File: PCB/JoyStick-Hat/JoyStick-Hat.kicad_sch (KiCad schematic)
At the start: 0 parts

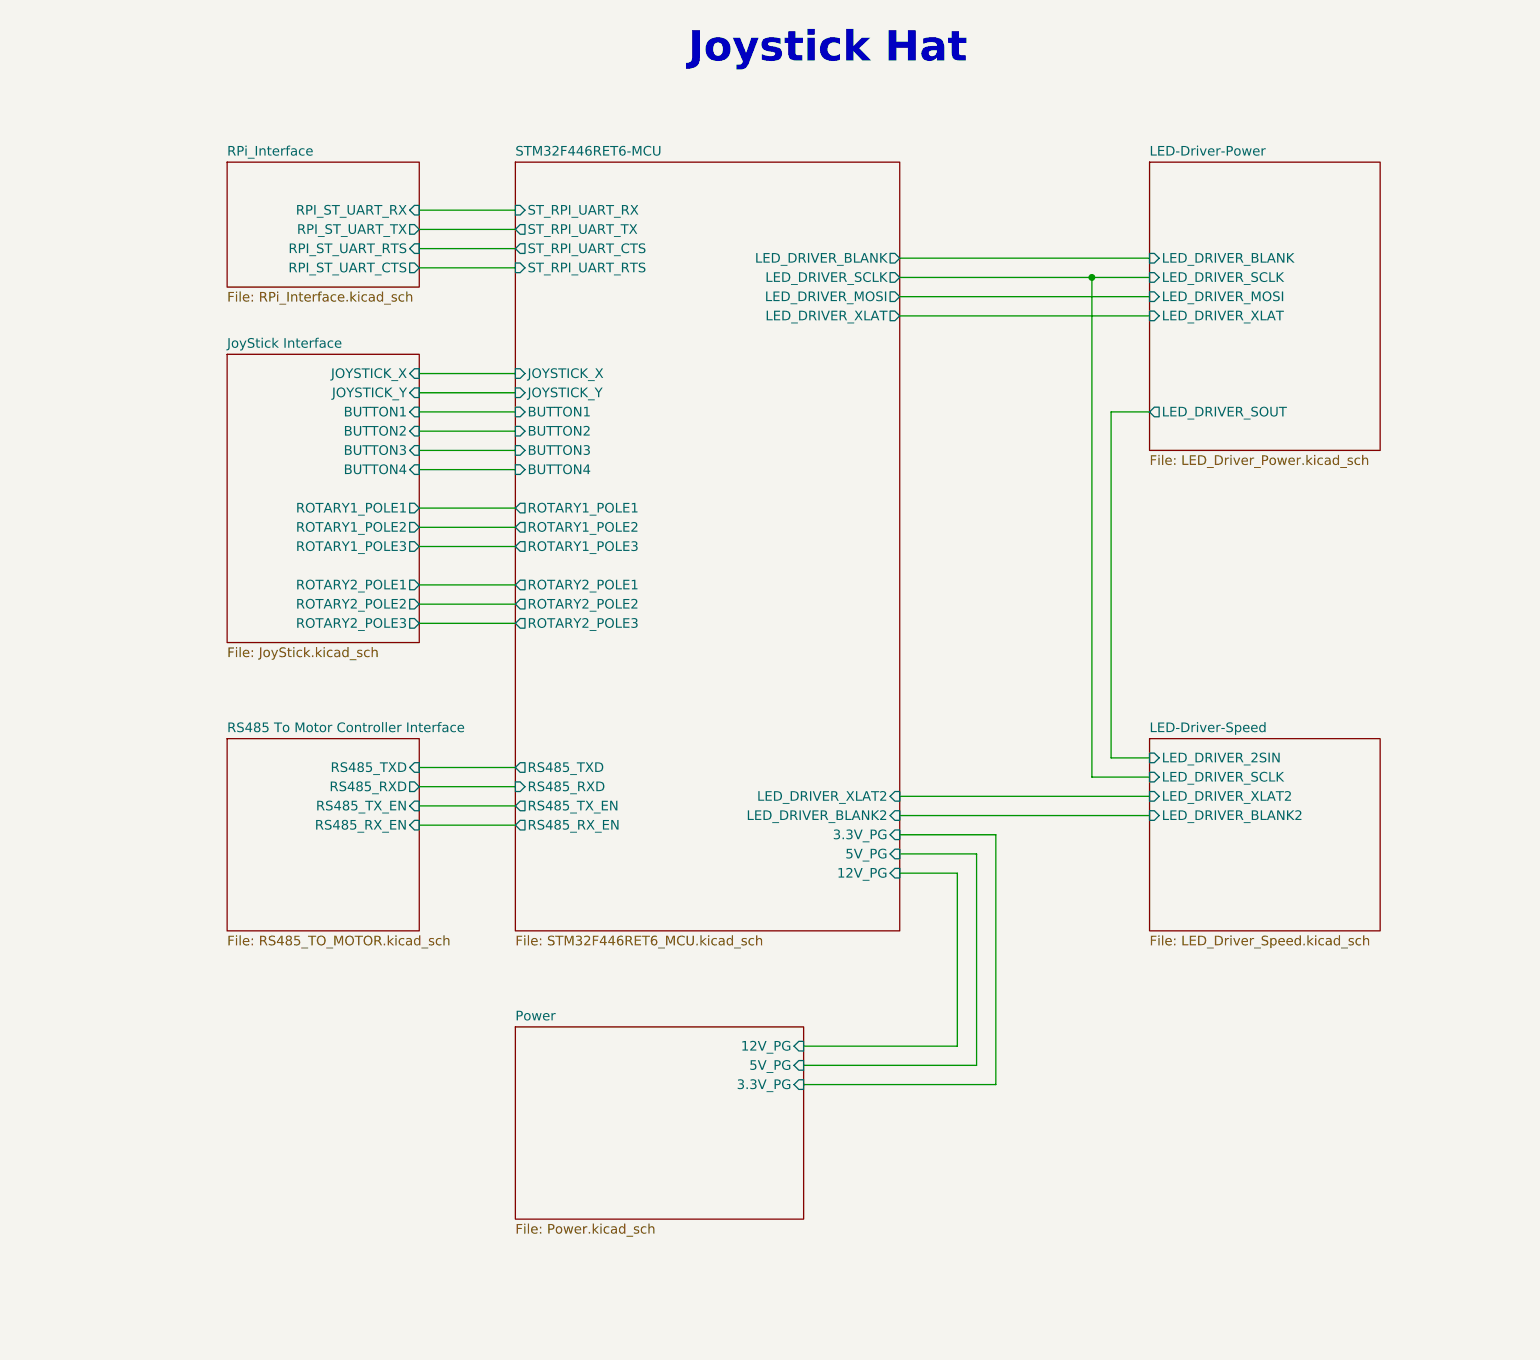
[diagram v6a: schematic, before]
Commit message: Design Rules, Component Placement. Features Dropped
Added design rules for OSHPark.com to PCB, Most components placed roughly for whole board more to follow and more tweaks,. Features were dropped/rearanged. USB for STM32 dropped as its not necessary. LED driver and LEDs will be on separate board and SPI will run through cabling via differential transceiver that has yet to be added to schematic.
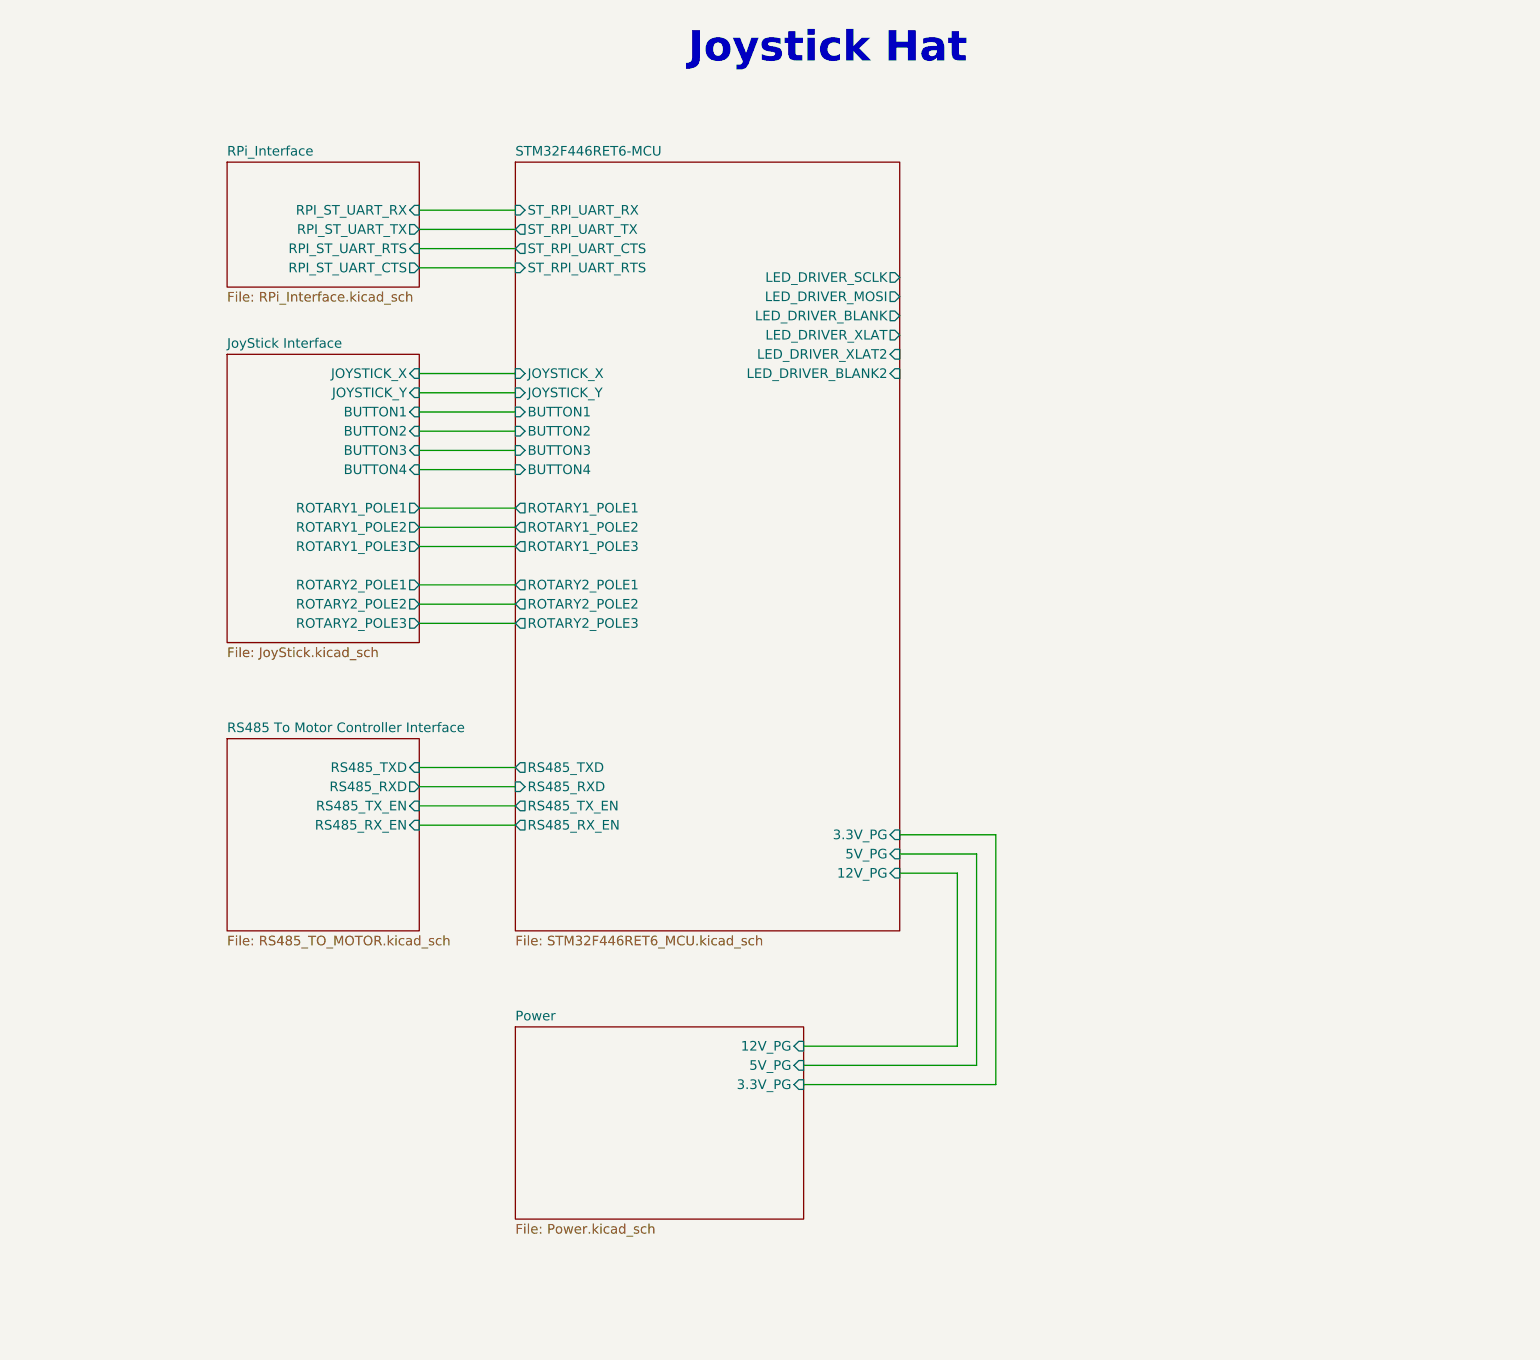
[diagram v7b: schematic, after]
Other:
- removed sheet LED-Driver-Power
- removed sheet LED-Driver-Speed
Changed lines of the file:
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@@
 (kicad_sch (version 20230121) (generator eeschema)
   (paper "A4")
-  (junction (at 190.5 53.34) (diameter 0) (color 0 0 0 0)
-  )
-  (wire (pts (xy 190.5 53.34) (xy 198.12 53.34))
-    (stroke (width 0) (type default))
-  )
   (wire (pts (xy 177.8 127) (xy 165.1 127))
     (stroke (width 0) (type default))
@@
     (stroke (width 0) (type default))
   )
-  (wire (pts (xy 165.1 58.42) (xy 198.12 58.42))
-    (stroke (width 0) (type default))
-  )
   (wire (pts (xy 101.6 86.36) (xy 114.3 86.36))
     (stroke (width 0) (type default))
@@
     (stroke (width 0) (type default))
   )
-  (wire (pts (xy 165.1 124.46) (xy 198.12 124.46))
-    (stroke (width 0) (type default))
-  )
   (wire (pts (xy 152.4 160.02) (xy 177.8 160.02))
     (stroke (width 0) (type default))
   )
-  (wire (pts (xy 193.04 71.12) (xy 198.12 71.12))
-    (stroke (width 0) (type default))
-  )
   (wire (pts (xy 101.6 71.12) (xy 114.3 71.12))
     (stroke (width 0) (type default))
   )
-  (wire (pts (xy 190.5 53.34) (xy 190.5 119.38))
-    (stroke (width 0) (type default))
-  )
   (wire (pts (xy 101.6 76.2) (xy 114.3 76.2))
     (stroke (width 0) (type default))
   )
-  (wire (pts (xy 165.1 121.92) (xy 198.12 121.92))
-    (stroke (width 0) (type default))
-  )
   (wire (pts (xy 177.8 160.02) (xy 177.8 127))
     (stroke (width 0) (type default))
   )
-  (wire (pts (xy 165.1 55.88) (xy 198.12 55.88))
-    (stroke (width 0) (type default))
-  )
   (wire (pts (xy 101.6 123.19) (xy 114.3 123.19))
     (stroke (width 0) (type default))
@@
     (stroke (width 0) (type default))
   )
-  (wire (pts (xy 190.5 119.38) (xy 198.12 119.38))
-    (stroke (width 0) (type default))
-  )
-  (wire (pts (xy 165.1 50.8) (xy 198.12 50.8))
-    (stroke (width 0) (type default))
-  )
-  (wire (pts (xy 198.12 116.84) (xy 193.04 116.84))
-    (stroke (width 0) (type default))
-  )
   (wire (pts (xy 175.26 157.48) (xy 175.26 129.54))
     (stroke (width 0) (type default))
@@
     (stroke (width 0) (type default))
   )
-  (wire (pts (xy 193.04 116.84) (xy 193.04 71.12))
-    (stroke (width 0) (type default))
-  )
   (wire (pts (xy 101.6 125.73) (xy 114.3 125.73))
     (stroke (width 0) (type default))
@@
   )
   (wire (pts (xy 101.6 49.53) (xy 114.3 49.53))
-    (stroke (width 0) (type default))
-  )
-  (wire (pts (xy 165.1 53.34) (xy 190.5 53.34))
     (stroke (width 0) (type default))
   )
@@
     (effects (font (size 4 4) (thickness 0.8) bold) (justify left bottom))
   )
-  (sheet (at 198.12 114.3) (size 30.48 25.4) (fields_autoplaced)
-    (stroke (width 0.1524) (type solid))
-    (fill (color 255 255 0 1.0000))
-    (property "Sheetname" "LED-Driver-Speed" (at 198.12 113.5884 0)
-      (effects (font (size 1.27 1.27)) (justify left bottom))
-    )
-    (property "Sheetfile" "LED_Driver_Speed.kicad_sch" (at 198.12 140.2846 0)
-      (effects (font (size 1.27 1.27)) (justify left top))
-    )
-    (pin "LED_DRIVER_SCLK" input (at 198.12 119.38 180)
-      (effects (font (size 1.27 1.27)) (justify left))
-    )
-    (pin "LED_DRIVER_2SIN" input (at 198.12 116.84 180)
-      (effects (font (size 1.27 1.27)) (justify left))
-    )
-    (pin "LED_DRIVER_BLANK2" input (at 198.12 124.46 180)
-      (effects (font (size 1.27 1.27)) (justify left))
-    )
-    (pin "LED_DRIVER_XLAT2" input (at 198.12 121.92 180)
-      (effects (font (size 1.27 1.27)) (justify left))
-    )
-    (instances
-      (project "JoyStick-Hat"
-        (path "/cf0c81b5-5bdf-47c3-83c0-f6980f515e65" (page "4"))
-      )
-    )
-  )
   (sheet (at 76.2 63.5) (size 25.4 38.1) (fields_autoplaced)
     (stroke (width 0.1524) (type solid))
@@
     )
   )
-  (sheet (at 198.12 38.1) (size 30.48 38.1) (fields_autoplaced)
-    (stroke (width 0.1524) (type solid))
-    (fill (color 255 255 0 1.0000))
-    (property "Sheetname" "LED-Driver-Power" (at 198.12 37.3884 0)
-      (effects (font (size 1.27 1.27)) (justify left bottom))
-    )
-    (property "Sheetfile" "LED_Driver_Power.kicad_sch" (at 198.12 76.7846 0)
-      (effects (font (size 1.27 1.27)) (justify left top))
-    )
-    (pin "LED_DRIVER_SOUT" output (at 198.12 71.12 180)
-      (effects (font (size 1.27 1.27)) (justify left))
-    )
-    (pin "LED_DRIVER_SCLK" input (at 198.12 53.34 180)
-      (effects (font (size 1.27 1.27)) (justify left))
-    )
-    (pin "LED_DRIVER_MOSI" input (at 198.12 55.88 180)
-      (effects (font (size 1.27 1.27)) (justify left))
-    )
-    (pin "LED_DRIVER_XLAT" input (at 198.12 58.42 180)
-      (effects (font (size 1.27 1.27)) (justify left))
-    )
-    (pin "LED_DRIVER_BLANK" input (at 198.12 50.8 180)
-      (effects (font (size 1.27 1.27)) (justify left))
-    )
-    (instances
-      (project "JoyStick-Hat"
-        (path "/cf0c81b5-5bdf-47c3-83c0-f6980f515e65" (page "3"))
-      )
-    )
-  )
   (sheet (at 114.3 152.4) (size 38.1 25.4) (fields_autoplaced)
     (stroke (width 0.1524) (type solid))
@@
       (effects (font (size 1.27 1.27)) (justify left))
     )
-    (pin "LED_DRIVER_BLANK" output (at 165.1 50.8 0)
+    (pin "LED_DRIVER_BLANK" output (at 165.1 58.42 0)
       (effects (font (size 1.27 1.27)) (justify right))
     )
@@
       (effects (font (size 1.27 1.27)) (justify right))
     )
-    (pin "LED_DRIVER_XLAT" output (at 165.1 58.42 0)
+    (pin "LED_DRIVER_XLAT" output (at 165.1 60.96 0)
       (effects (font (size 1.27 1.27)) (justify right))
     )
@@
       (effects (font (size 1.27 1.27)) (justify right))
     )
-    (pin "LED_DRIVER_BLANK2" input (at 165.1 124.46 0)
-      (effects (font (size 1.27 1.27)) (justify right))
-    )
-    (pin "LED_DRIVER_XLAT2" input (at 165.1 121.92 0)
-      (effects (font (size 1.27 1.27)) (justify right))
-    )
+    (pin "LED_DRIVER_BLANK2" input (at 165.1 66.04 0)
+      (effects (font (size 1.27 1.27)) (justify right))
+    )
+    (pin "LED_DRIVER_XLAT2" input (at 165.1 63.5 0)
+      (effects (font (size 1.27 1.27)) (justify right))
+    )
